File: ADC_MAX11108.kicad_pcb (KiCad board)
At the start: 4 copper layers, 100 x 100 mm, 317 parts, among them IC1 MAX11108AVB+T, IC10 MAX11108AVB+T, IC11 MAX11108AVB+T, IC12 MAX11108AVB+T, IC13 MAX11108AVB+T, IC14 MAX11108AVB+T, IC15 MAX11108AVB+T, IC16 MAX11108AVB+T, IC17 MAX11108AVB+T, IC18 MAX11108AVB+T, IC19 MAX11108AVB+T, IC2 MAX11108AVB+T, IC20 MAX11108AVB+T, IC21 MAX11108AVB+T, IC22 524SDCGI8, IC23 MAX11108AVB+T, IC24 524SDCGI8, IC25 MAX11108AVB+T, IC26 524SDCGI8, IC27 MAX11108AVB+T, IC28 524SDCGI8, IC29 MAX11108AVB+T, IC3 MAX11108AVB+T, IC30 LMS1585ACSX-ADJ_NOPB, IC4 MAX11108AVB+T, IC5 MAX11108AVB+T, IC6 MAX11108AVB+T, IC7 MAX11108AVB+T, IC8 MAX11108AVB+T, IC9 MAX11108AVB+T, J1 Conn_01x02_Pin, J2 Conn_01x02_Pin, J3 Conn_01x07_Pin, J4 Conn_01x07_Pin, J5 Conn_01x07_Pin, J6 Conn_01x08_Pin, J7 Conn_01x08_Pin, J8 Conn_01x02_Pin, Q1 LMS1587CT-3.3_NOPB

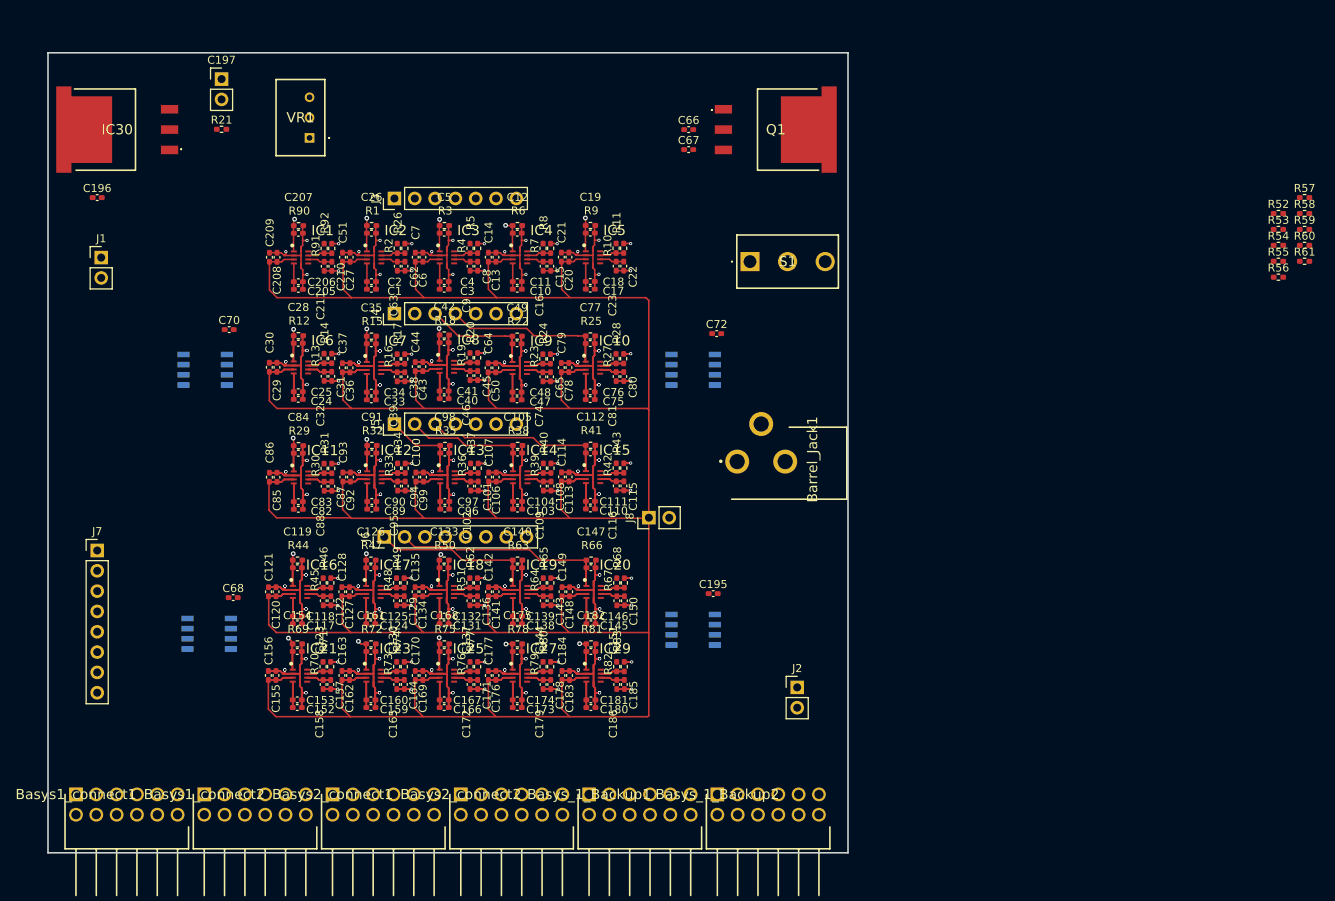
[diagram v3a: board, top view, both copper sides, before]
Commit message: Finished Power section routing, added LED indicators
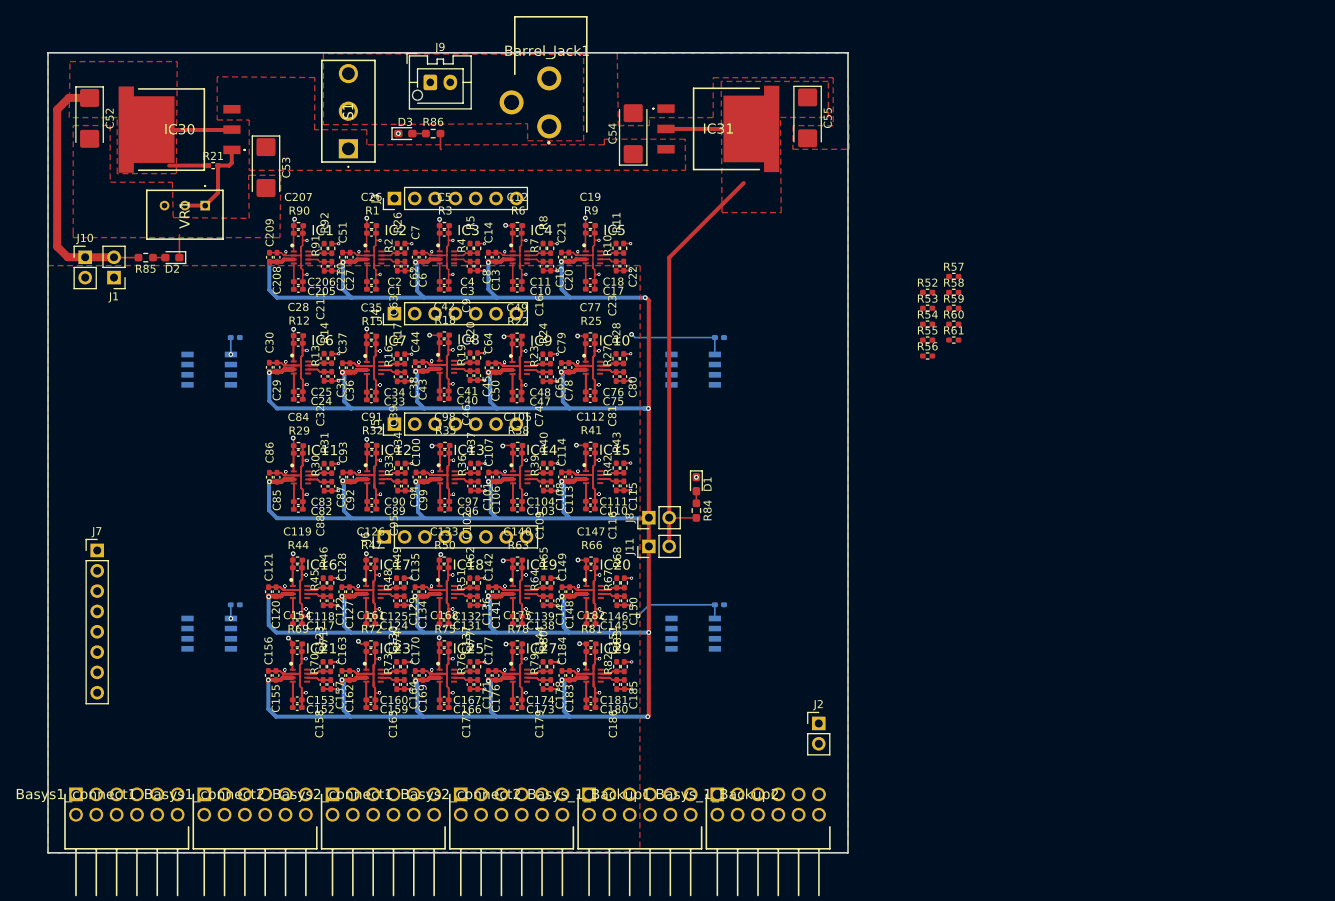
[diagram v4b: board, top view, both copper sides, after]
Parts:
- removed C196, C66, C67: 10uF, Capacitor_SMD:C_0402_1005Metric_Pad0.74x0.62mm_HandSolder
- removed C197: 10uF, Connector_PinHeader_2.54mm:PinHeader_1x02_P2.54mm_Vertical
- removed Q1: LMS1587CT-3.3_NOPB, My_footprints:LM1085ISX33NOPB
- added C52: 10uF Tantalum, Capacitor_Tantalum_SMD:CP_EIA-6032-28_Kemet-C_HandSolder, F.Cu at (105.0, 57.1)
- added C53: 10uF Tantalum, Capacitor_Tantalum_SMD:CP_EIA-6032-28_Kemet-C_HandSolder, F.Cu at (127.1, 63.2)
- added C54: 10uF Tantalum, Capacitor_Tantalum_SMD:CP_EIA-6032-28_Kemet-C_HandSolder, F.Cu at (173.0, 59.0)
- added C55: 10uF Tantalum, Capacitor_Tantalum_SMD:CP_EIA-6032-28_Kemet-C_HandSolder, F.Cu at (194.8, 57.0)
- added D1: RED LED, LED_SMD:LED_0603_1608Metric_Pad1.05x0.95mm_HandSolder, F.Cu at (180.9, 102.8)
- added D2: RED LED, LED_SMD:LED_0603_1608Metric_Pad1.05x0.95mm_HandSolder, F.Cu at (115.4, 74.5)
- added D3: GREEN LED, LED_SMD:LED_0603_1608Metric_Pad1.05x0.95mm_HandSolder, F.Cu at (144.5, 59.0)
- added IC31: LMS1587CS-3.3, SamacSys_Parts:LMS1587CSXADJNOPB, F.Cu at (184.9, 58.4)
- added J10: Conn_01x02_Pin, Connector_PinHeader_2.54mm:PinHeader_1x02_P2.54mm_Vertical, F.Cu at (104.5, 74.5)
- added J11: Conn_01x02_Pin, Connector_PinHeader_2.54mm:PinHeader_1x02_P2.54mm_Vertical, F.Cu at (175.0, 110.6)
- added J9: Conn_01x02_Pin, Connector_JST:JST_XA_B02B-XASK-1-A_1x02_P2.50mm_Vertical, F.Cu at (147.6, 52.6)
- added R84: 120, Resistor_SMD:R_0603_1608Metric_Pad0.98x0.95mm_HandSolder, F.Cu at (180.9, 106.1)
- added R85: 120, Resistor_SMD:R_0603_1608Metric_Pad0.98x0.95mm_HandSolder, F.Cu at (112.1, 74.5)
- added R86: 470, Resistor_SMD:R_0603_1608Metric_Pad0.98x0.95mm_HandSolder, F.Cu at (148.0, 59.0)
- C195, C68, C70, C72: moved to B.Cu
- IC30: value LMS1585ACSX-ADJ_NOPB -> LMS1587CS-ADJ; footprint My_footprints:LM1085ISX33NOPB -> SamacSys_Parts:LMS1587CSXADJNOPB
- moved S1 52.1 mm to (137.4, 60.9), turned to 90 degrees
- moved Barrel_Jack1 51.0 mm to (158.2, 55.1), turned to 0 degrees
- moved R57 44.9 mm to (213.1, 76.8)
- moved R58 44.9 mm to (213.1, 78.8)
- moved R59 44.9 mm to (213.1, 80.8)
- moved R60 44.9 mm to (213.1, 82.8)
- moved R61 44.9 mm to (213.1, 84.8)
- moved R52 44.9 mm to (209.8, 78.8)
- moved R53 44.9 mm to (209.8, 80.8)
- moved R54 44.9 mm to (209.8, 82.8)
- moved R55 44.9 mm to (209.8, 84.8)
- moved R56 44.9 mm to (209.8, 86.8)
- moved C70 34.4 mm to (123.3, 117.9)
- moved C72 33.9 mm to (183.8, 117.9)
- moved C68 32.5 mm to (123.3, 84.5)
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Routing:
- net Vref_LDO: track 0.00 -> 62.4 mm
- net Net-(IC30-OUTPUT): track 0.00 -> 47.1 mm
- net 3.3_ADJ: track 283.8 -> 312.2 mm, vias 0 -> 4
- net Net-(IC30-ADJ/GND): track 0.00 -> 11.6 mm
- net GND: track 746.0 -> 748.8 mm, vias 185 -> 187
- net Switch_out: track 0.00 -> 2.04 mm
- net Net-(D3-A): track 0.00 -> 1.70 mm
- net 3.3VRef: track 549.3 -> 551.0 mm, vias 0 -> 28
- net Net-(D2-A): track 0.00 -> 1.55 mm
- net Net-(D1-A): track 0.00 -> 1.51 mm
- net Ain_11: track 38.4 -> 39.8 mm
- net Ain_20: track 30.4 -> 31.8 mm, vias 0 -> 1
- net Ain_15: track 26.4 -> 27.6 mm, vias 0 -> 1
- net Ain_13: track 13.3 -> 14.3 mm, vias 0 -> 1
- net Ain_9: track 17.3 -> 17.5 mm, vias 0 -> 1
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- added copper zone on F.Cu, net 3.3_ADJ
- added copper zone on B.Cu, net GND
- added copper zone on F.Cu, net GND
- added copper zone on F.Cu, net Net-(IC30-OUTPUT)
- added copper zone on F.Cu, net Power_In
- added copper zone on F.Cu, net Switch_out
- added copper zone on F.Cu, net Vref_LDO

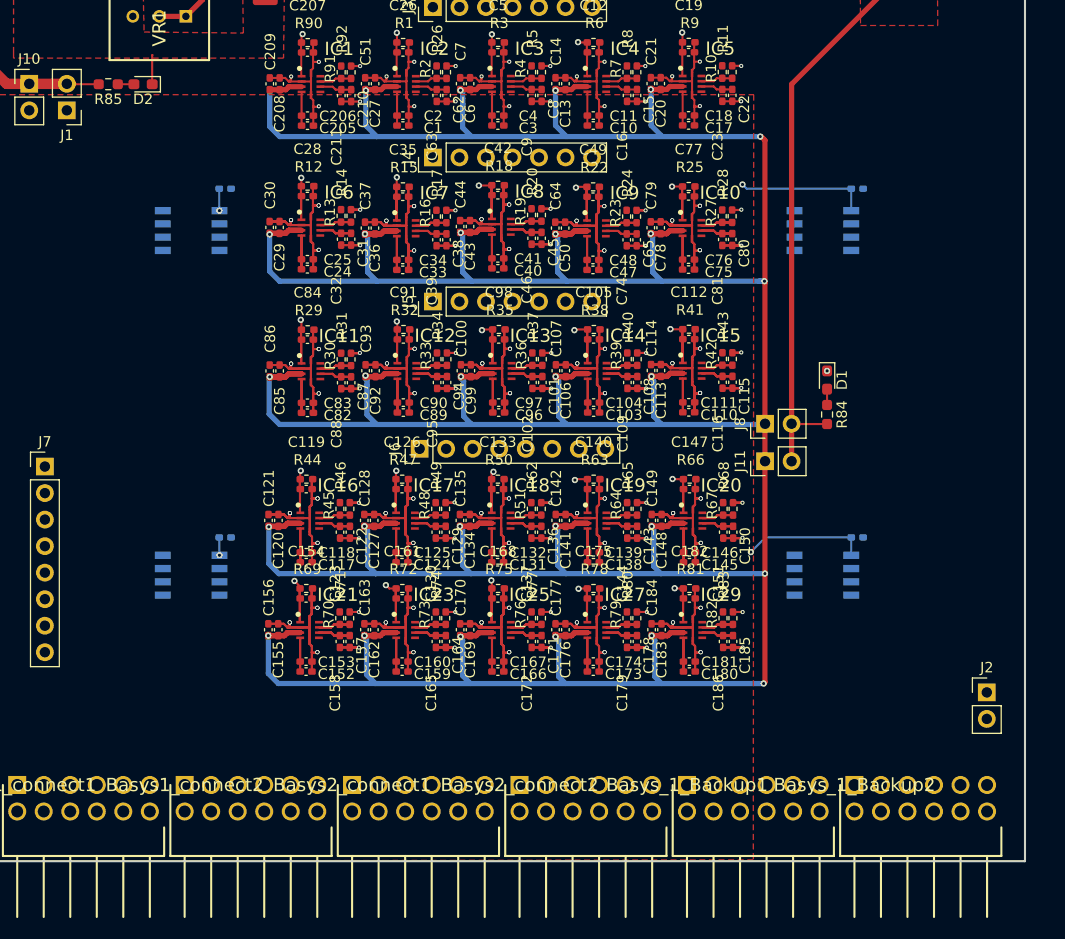
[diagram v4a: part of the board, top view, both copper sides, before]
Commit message: Routed most of the Douts, and all of the CS & SCLK
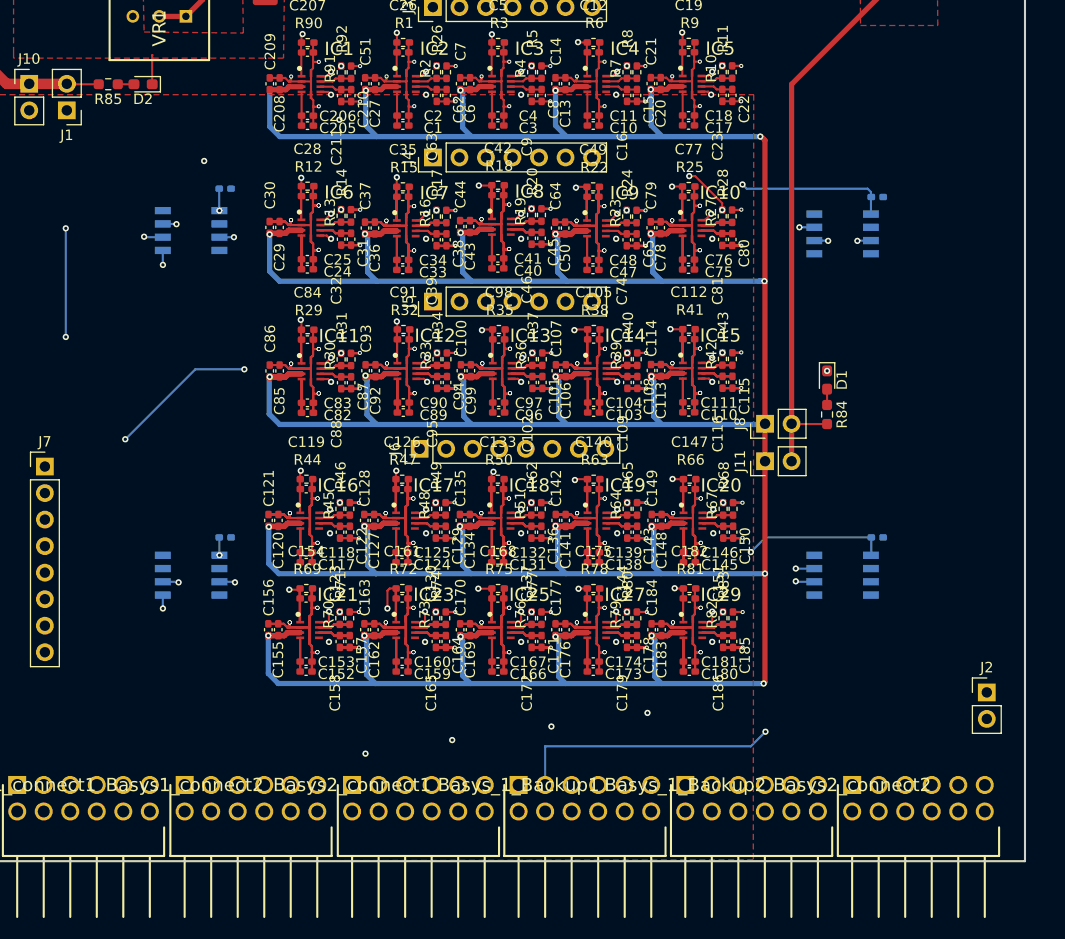
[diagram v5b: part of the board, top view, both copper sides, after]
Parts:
- moved Basys2_connect2 31.9 mm to (183.3, 141.6)
- moved Basys_1_Backup2 16.2 mm to (167.3, 141.6)
- moved Basys_1_Backup1 16.1 mm to (151.4, 141.6)
- moved C195 2.08 mm to (185.7, 85.3)
- moved C72 1.92 mm to (185.7, 117.9)
- moved IC24 1.92 mm to (182.4, 88.8)
- moved IC26 1.89 mm to (182.4, 121.5)
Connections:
- IC26 pad 3: unconnected-(IC26-Q1-Pad3) -> CLK_4
- IC26 pad 7: CLK_4 -> unconnected-(IC26-Q3-Pad7)
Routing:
- net /Dout5: track 0.00 -> 153.1 mm, vias 0 -> 1
- net /Dout4: track 0.00 -> 151.7 mm, vias 0 -> 1
- net /Dout10: track 0.00 -> 132.3 mm, vias 0 -> 5
- net /Dout9: track 0.00 -> 116.5 mm, vias 0 -> 1
- net /Dout3: track 0.00 -> 110.0 mm, vias 0 -> 2
- net /Dout8: track 0.00 -> 107.9 mm, vias 0 -> 1
- net Dout14: track 0.00 -> 103.4 mm, vias 0 -> 3
- net /Dout2: track 0.00 -> 101.8 mm, vias 0 -> 1
- net /Dout7: track 0.00 -> 95.8 mm, vias 0 -> 1
- net CS_3: track 0.00 -> 93.0 mm, vias 0 -> 6
- net Dout13: track 0.00 -> 90.5 mm, vias 0 -> 1
- net CS_2: track 0.00 -> 90.4 mm, vias 0 -> 6
- net /Dout1: track 0.00 -> 90.0 mm, vias 0 -> 1
- net /Dout6: track 0.00 -> 87.3 mm, vias 0 -> 1
- net CS_1: track 0.00 -> 86.8 mm, vias 0 -> 6
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
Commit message: added GND Vias
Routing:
- net GND: vias 187 -> 195
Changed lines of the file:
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@@
+	)
+	(via
+		(at 126.4 68.4)
+		(size 0.6)
+		(drill 0.3)
+		(layers "F.Cu" "B.Cu")
+		(free yes)
+		(net 30)
 	)
 	(via
@@
 	)
 	(via
+		(at 197.6 60.2)
+		(size 0.6)
+		(drill 0.3)
+		(layers "F.Cu" "B.Cu")
+		(free yes)
+		(net 30)
+	)
+	(via
 		(at 136.160728 103.62625)
 		(size 0.4)
@@
 	)
 	(via
+		(at 172.4 53.4)
+		(size 0.6)
+		(drill 0.3)
+		(layers "F.Cu" "B.Cu")
+		(free yes)
+		(net 30)
+	)
+	(via
 		(at 168.793228 128.885)
 		(size 0.4)
@@
 		(size 0.4)
 		(drill 0.2)
+		(layers "F.Cu" "B.Cu")
+		(free yes)
+		(net 30)
+	)
+	(via
+		(at 173.6 53.4)
+		(size 0.6)
+		(drill 0.3)
+		(layers "F.Cu" "B.Cu")
+		(free yes)
+		(net 30)
+	)
+	(via
+		(at 197.6 58.9)
+		(size 0.6)
+		(drill 0.3)
 		(layers "F.Cu" "B.Cu")
 		(free yes)
@@
 	)
 	(via
+		(at 104.3 62.4)
+		(size 0.6)
+		(drill 0.3)
+		(layers "F.Cu" "B.Cu")
+		(free yes)
+		(net 30)
+	)
+	(via
 		(at 166.065728 87.54125)
 		(size 0.4)
@@
 	)
 	(via
+		(at 105.8 62.4)
+		(size 0.6)
+		(drill 0.3)
+		(layers "F.Cu" "B.Cu")
+		(free yes)
+		(net 30)
+	)
+	(via
 		(at 159.628228 99.83125)
 		(size 0.4)
@@
 		(layers "F.Cu" "B.Cu")
 		(free yes)
+		(net 30)
+	)
+	(via
+		(at 127.7 68.4)
+		(size 0.6)
+		(drill 0.3)
+		(layers "F.Cu" "B.Cu")
+		(free yes)

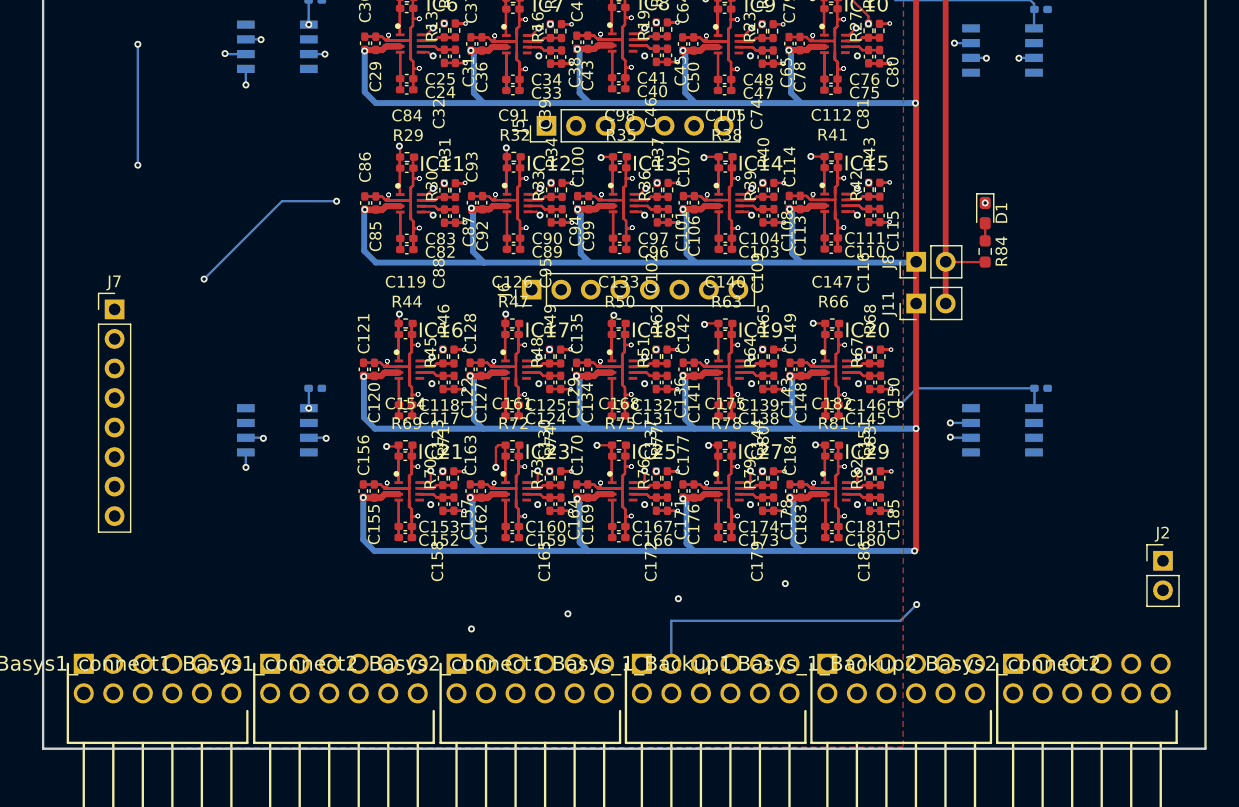
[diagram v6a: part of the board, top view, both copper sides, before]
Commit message: added routing for the connectors
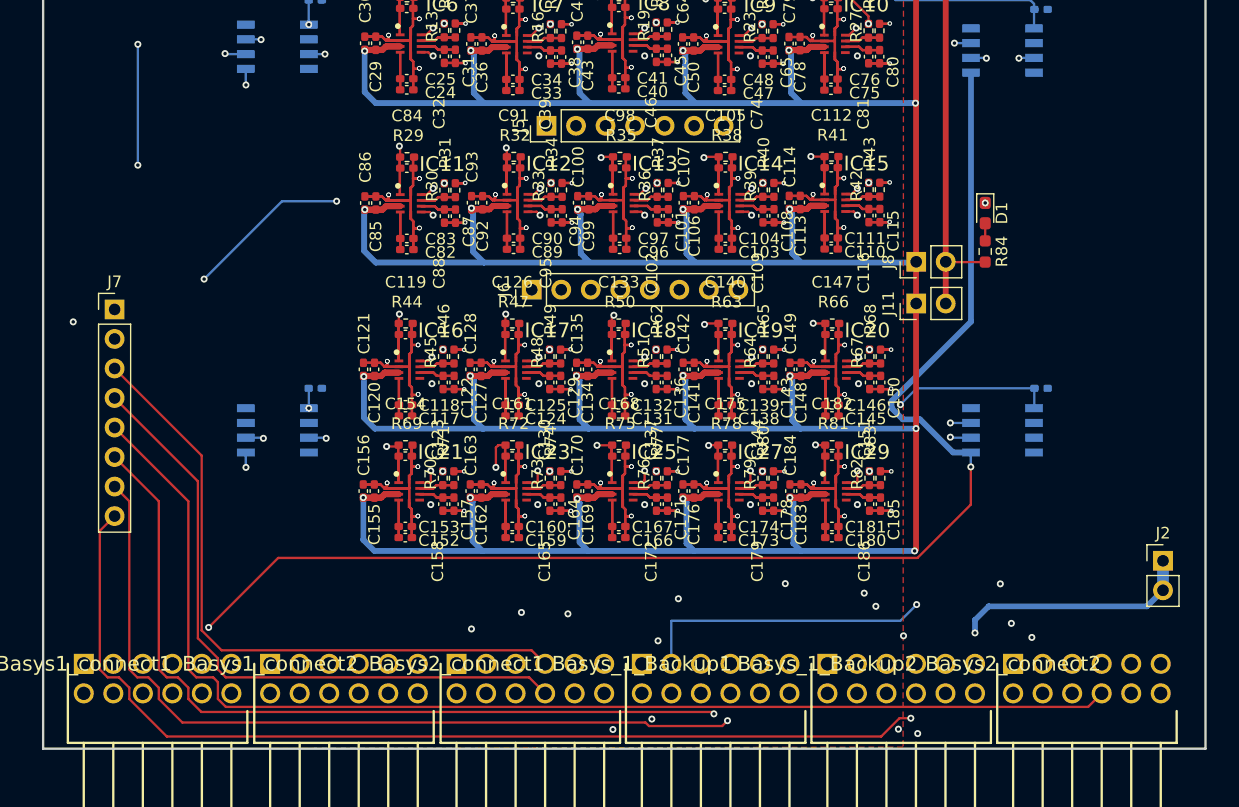
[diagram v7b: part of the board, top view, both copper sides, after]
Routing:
- net Serial_CLK: track 0.00 -> 119.0 mm, vias 0 -> 2
- net Basys_3.3V: track 0.00 -> 109.6 mm, vias 0 -> 1
- net B2_C2_8: track 0.00 -> 104.7 mm
- net B1_B2_8: track 0.00 -> 89.4 mm, vias 0 -> 1
- net B1_B1_7: track 0.00 -> 74.7 mm, vias 0 -> 1
- net B1_B1_8: track 0.00 -> 72.9 mm, vias 0 -> 1
- net B2_C1_7: track 0.00 -> 56.4 mm
- net B2_C1_8: track 0.00 -> 56.0 mm
- net B1C2_8: track 0.00 -> 46.7 mm
- net B1C1_8: track 0.00 -> 46.1 mm, vias 0 -> 1
- net Dout19: track 30.4 -> 54.8 mm, vias 1 -> 3
- net Dout21: track 49.0 -> 72.0 mm, vias 2 -> 4
- net Dout13: track 90.5 -> 111.6 mm, vias 1 -> 2
- net Dout22: track 46.0 -> 66.7 mm, vias 2 -> 3
- net Dout24: track 27.6 -> 48.2 mm, vias 2 -> 3
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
